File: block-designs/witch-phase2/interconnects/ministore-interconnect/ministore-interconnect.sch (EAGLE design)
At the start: 14 parts

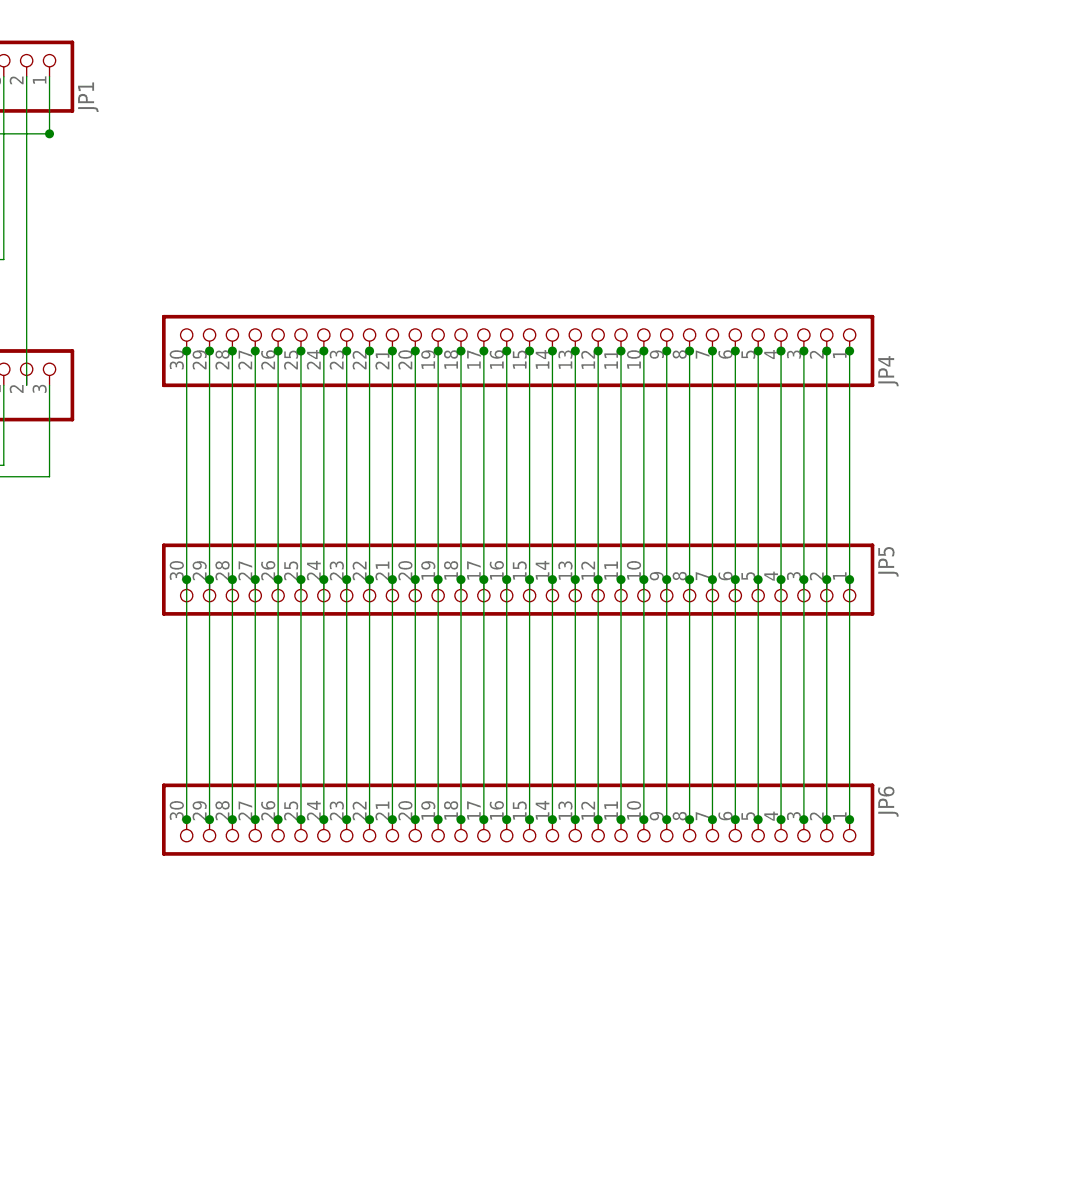
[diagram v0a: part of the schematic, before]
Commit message: fixes for layout and connections
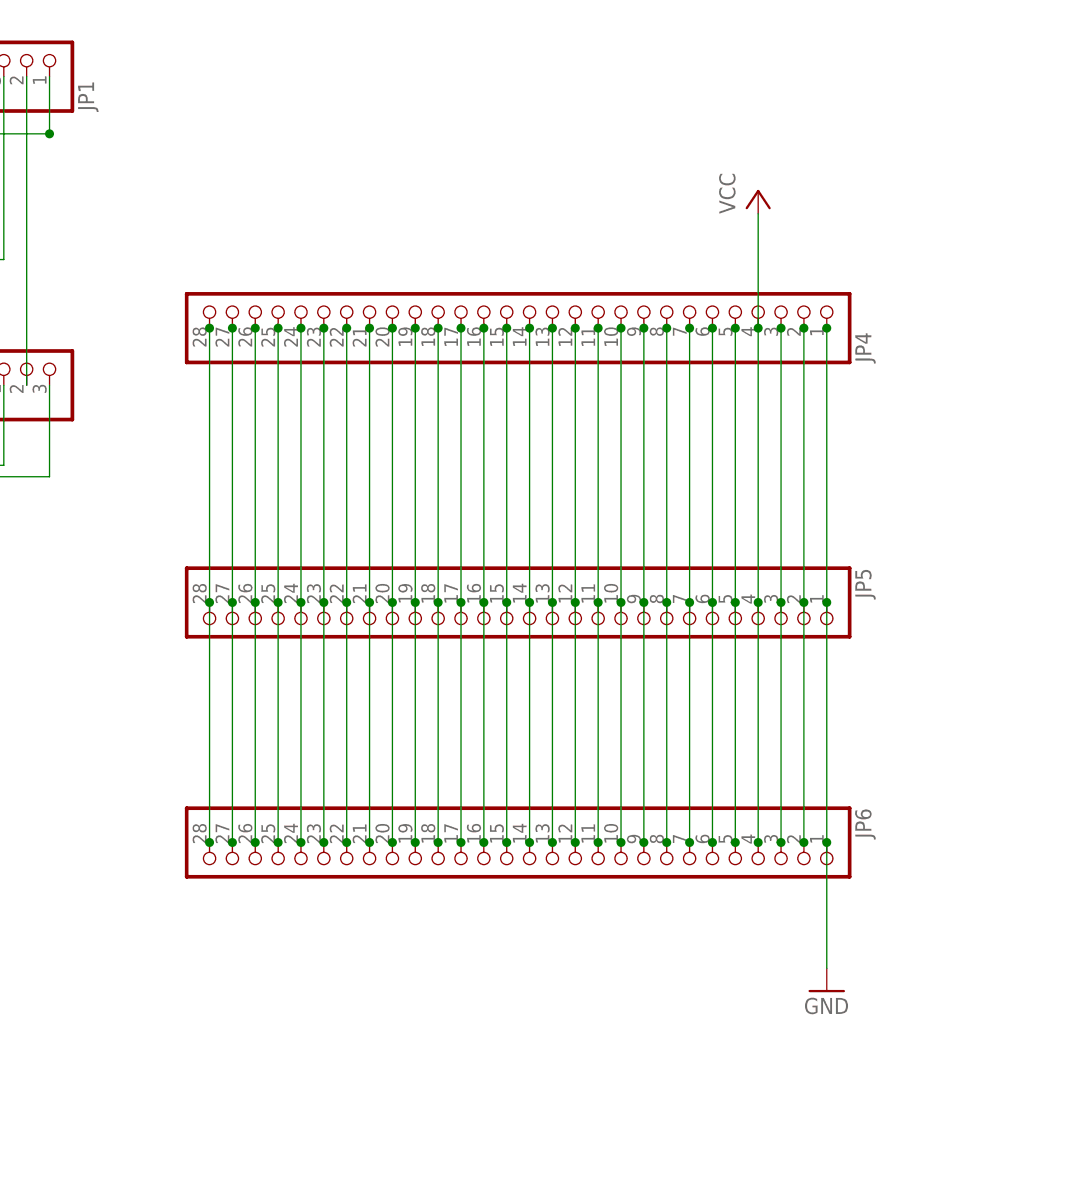
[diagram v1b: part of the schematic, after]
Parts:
- JP4, JP5, JP6: device pinhead:PINHD-1X30 -> pinhead:PINHD-1X28
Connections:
- removed net N$1: JP4.30, JP5.30, JP6.30
- removed net N$2: JP4.29, JP5.29, JP6.29
- removed net N$27: JP4.4, JP5.4, JP6.4
- removed net N$30: JP4.1, JP5.1, JP6.1
- net GND: now also JP4.1, JP5.1, JP6.1
- net VCC: now also JP4.4, JP5.4, JP6.4
